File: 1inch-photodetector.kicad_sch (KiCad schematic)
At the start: 21 parts, among them J1 Conn_01x03, J2 Conn_Coaxial, U1 ADA4898-2, U2 LT3032-12

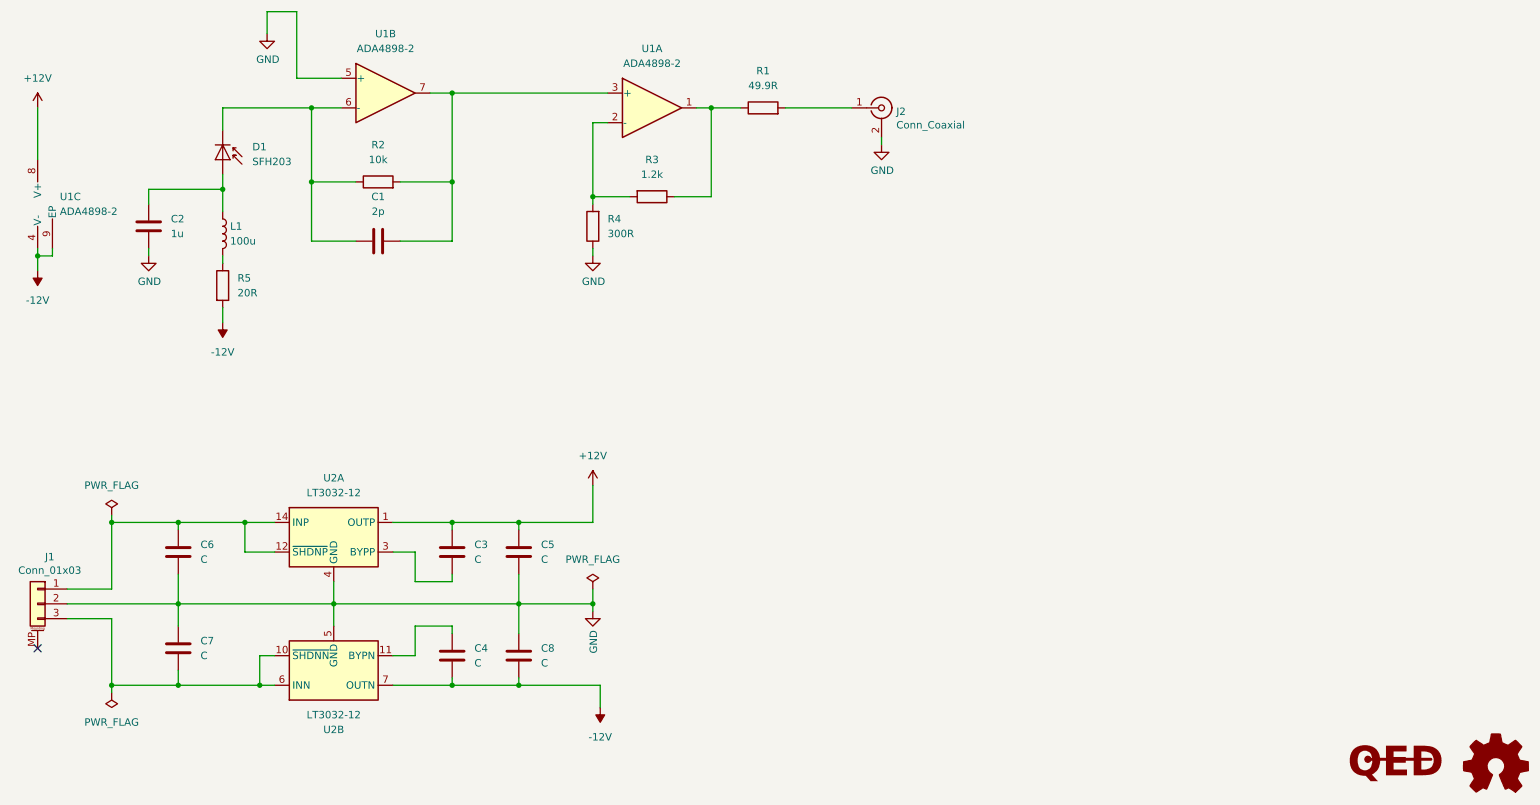
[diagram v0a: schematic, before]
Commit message: Disconnect GND from Earth by default (#10)
* Removed GND-Earth connection
  - Added optional jumpers to connect GND to Earth
  - Added more ground stitching vias
* Increased size to 25.4 mm
* Added comments regarding tolerances
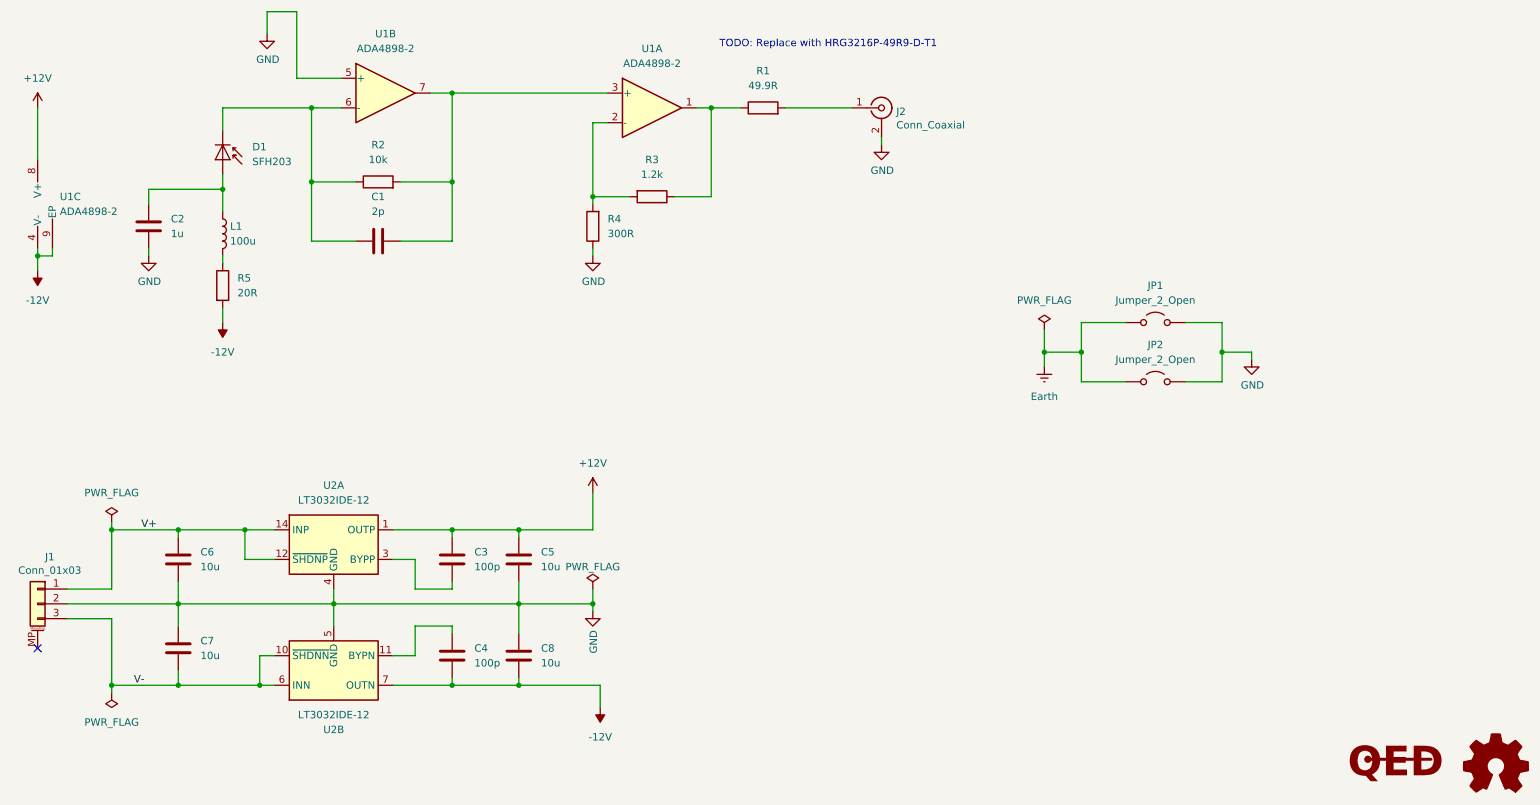
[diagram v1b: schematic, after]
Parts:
- added JP1, JP2: Jumper_2_Open, Resistor_SMD:R_0402_1005Metric, symbol Jumper:Jumper_2_Open
- C1: MFN (none) -> Yageo; PN (none) -> AC0603BRNPO9BN2R0; RoHS (none) -> Yes; Temperature (none) -> Top = –55 °C to 125 °C
- C2, L1: Temperature -55,125 -> Top = –55 °C to 125 °C
- C3, C4: value C -> 100p; MFN (none) -> Murata Electronics; PN (none) -> GCM1885C2A101JA16D; RoHS (none) -> Yes; Temperature (none) -> Top = –55 °C to 125 °C
- C5, C6, C7, C8: value C -> 10u; MFN (none) -> TDK; PN (none) -> CGA4J1X7S1E106K125AC; RoHS (none) -> Yes; Temperature (none) -> Top = –55 °C to 125 °C
- D1: MFN (none) -> ams Osram; PN (none) -> SFH 203 FA; RoHS (none) -> Yes; Temperature (none) -> Top = –40 °C to 100 °C; Tstorage = –40 °C to 100 °C
- J1: MFN (none) -> Molex; PN (none) -> 53398-0371; RoHS (none) -> Yes; Temperature (none) -> Top = –40 °C to 105 °C; Tstorage = –5 °C to 35 °C
- J2: MFN (none) -> TE Connectivity; PN (none) -> CONSMP001-SMD-G-T; RoHS (none) -> Yes; Temperature (none) -> Tstorage = –65 °C to 155 °C
- R1: footprint Resistor_SMD:R_0603_1608Metric -> Resistor_SMD:R_1206_3216Metric; MFN (none) -> Yageo; PN (none) -> HRG3216P-49R9-D-T1; RoHS (none) -> Yes; Temperature (none) -> Top = –55 °C to 155 °C
- R2: MFN (none) -> Susumu; PN (none) -> RG1608P-103-D-T5; RoHS (none) -> Yes; Temperature (none) -> Top = –55 °C to 155 °C
- R3: MFN (none) -> Susumu; PN (none) -> RG1608P-122-D-T5; RoHS (none) -> Yes; Temperature (none) -> Top = –55 °C to 155 °C
- R4: MFN (none) -> Susumu; PN (none) -> RG1608P-301-B-T5; RoHS (none) -> Yes; Temperature (none) -> Top = –55 °C to 155 °C
- R5: MFN (none) -> Susumu; PN (none) -> RG1608Q-200-D-T5; RoHS (none) -> Yes; Temperature (none) -> Top = –55 °C to 155 °C
- U1: Alternative (none) -> Analog Devices ADA4898-2YRDZ-R7; MFN (none) -> Analog Devices; PN (none) -> ADA4898-2YRDZ; RoHS (none) -> Yes; Temperature (none) -> Top = –40 °C to 105 °C; Tstorage = –65 °C to 150 °C
- U2: value LT3032-12 -> LT3032IDE-12; Alternative (none) -> Analog Devices LT3032EDE-12#PBF; MFN (none) -> Analog Devices; PN (none) -> LT3032IDE-12#PBF; RoHS (none) -> Yes; Temperature (none) -> Top = –40 °C to 125 °C
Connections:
- net GND: now also JP1.2 (B), JP2.2 (B)
- net V+: now reaches C6.1, J1.1 (Pin_1), U2.12 (~{SHDNP}), U2.14 (INP)
- net V-: now reaches C7.2, J1.3 (Pin_3), U2.10 (~{SHDNN}), U2.6 (INN), U2.9 (INN)
- new net Earth: JP1.1 (A), JP2.1 (A)
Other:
- note added: "TODO: Replace with HRG3216P-49R9-D-T1"
- moved on the sheet: C3, C5, C6, U2A
